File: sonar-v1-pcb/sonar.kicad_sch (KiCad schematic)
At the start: 1 part, among them J101 DF40C-80DS-0.4V51

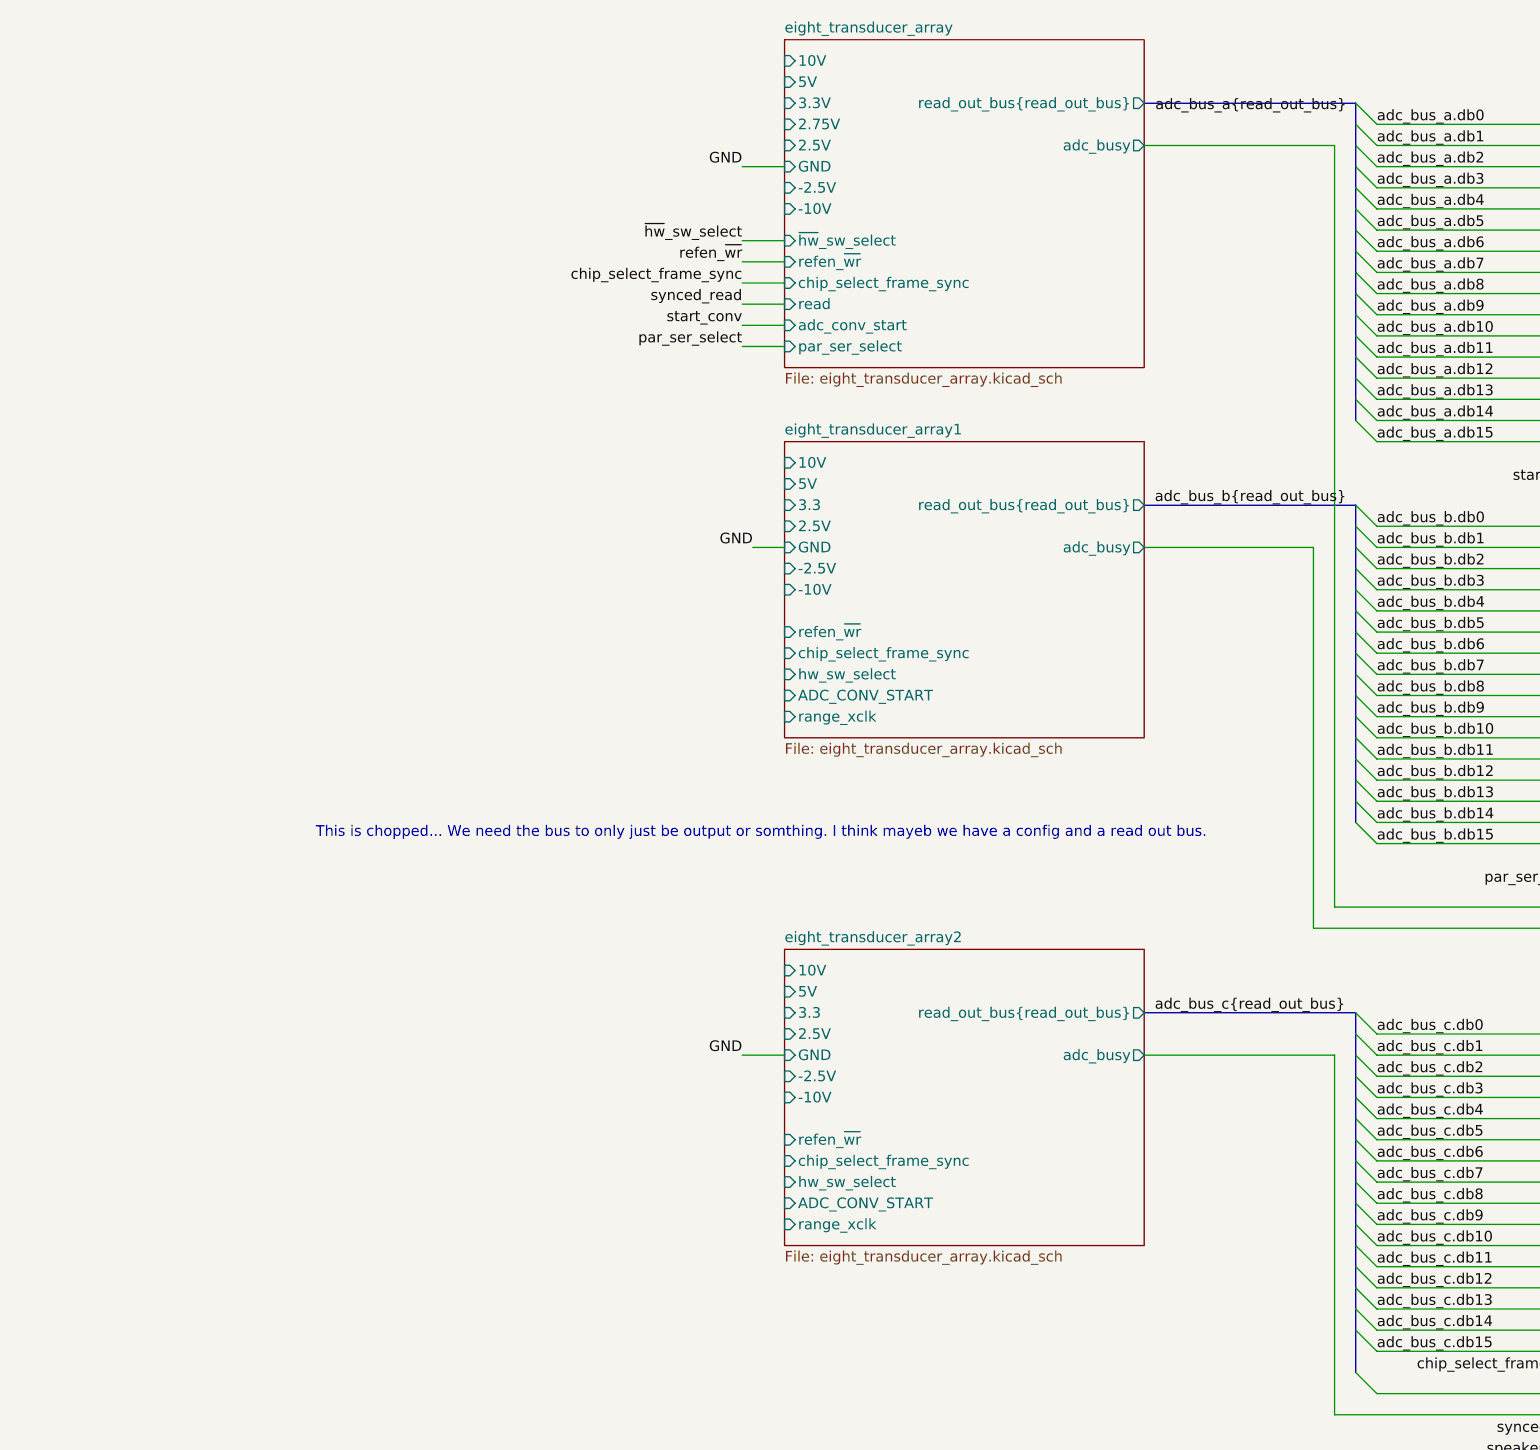
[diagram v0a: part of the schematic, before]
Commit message: Fix pinout
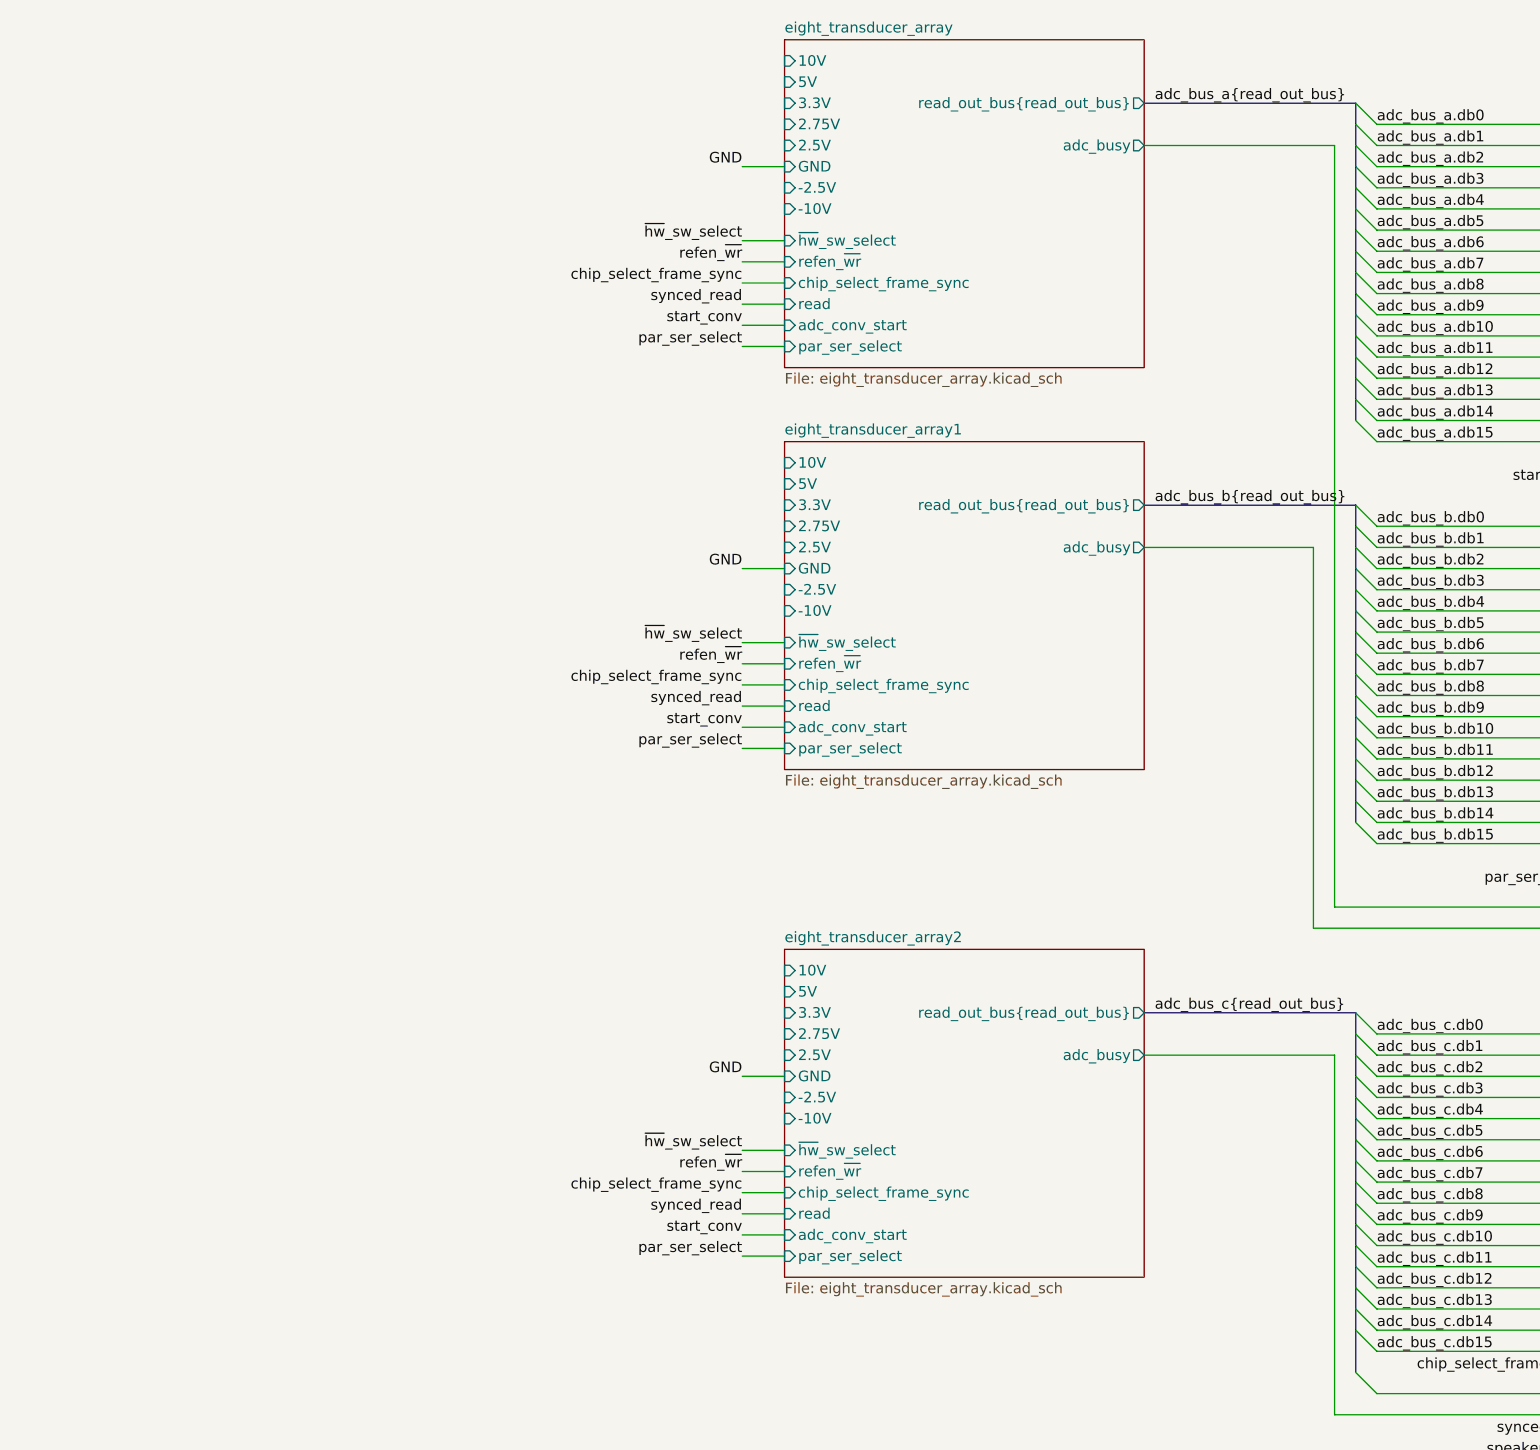
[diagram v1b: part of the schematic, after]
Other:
- sheet eight_transducer_array1 ports: added 2.75V, 3.3V, adc_conv_start, par_ser_select, read, ~{hw}_sw_select; removed 3.3, ADC_CONV_START, hw_sw_select, range_xclk
- sheet eight_transducer_array2 ports: added 2.75V, 3.3V, adc_conv_start, par_ser_select, read, ~{hw}_sw_select; removed 3.3, ADC_CONV_START, hw_sw_select, range_xclk
- note removed: "This is chopped... We need the bus to only just be output or somthing. I think mayeb we have a config and a read out bus."

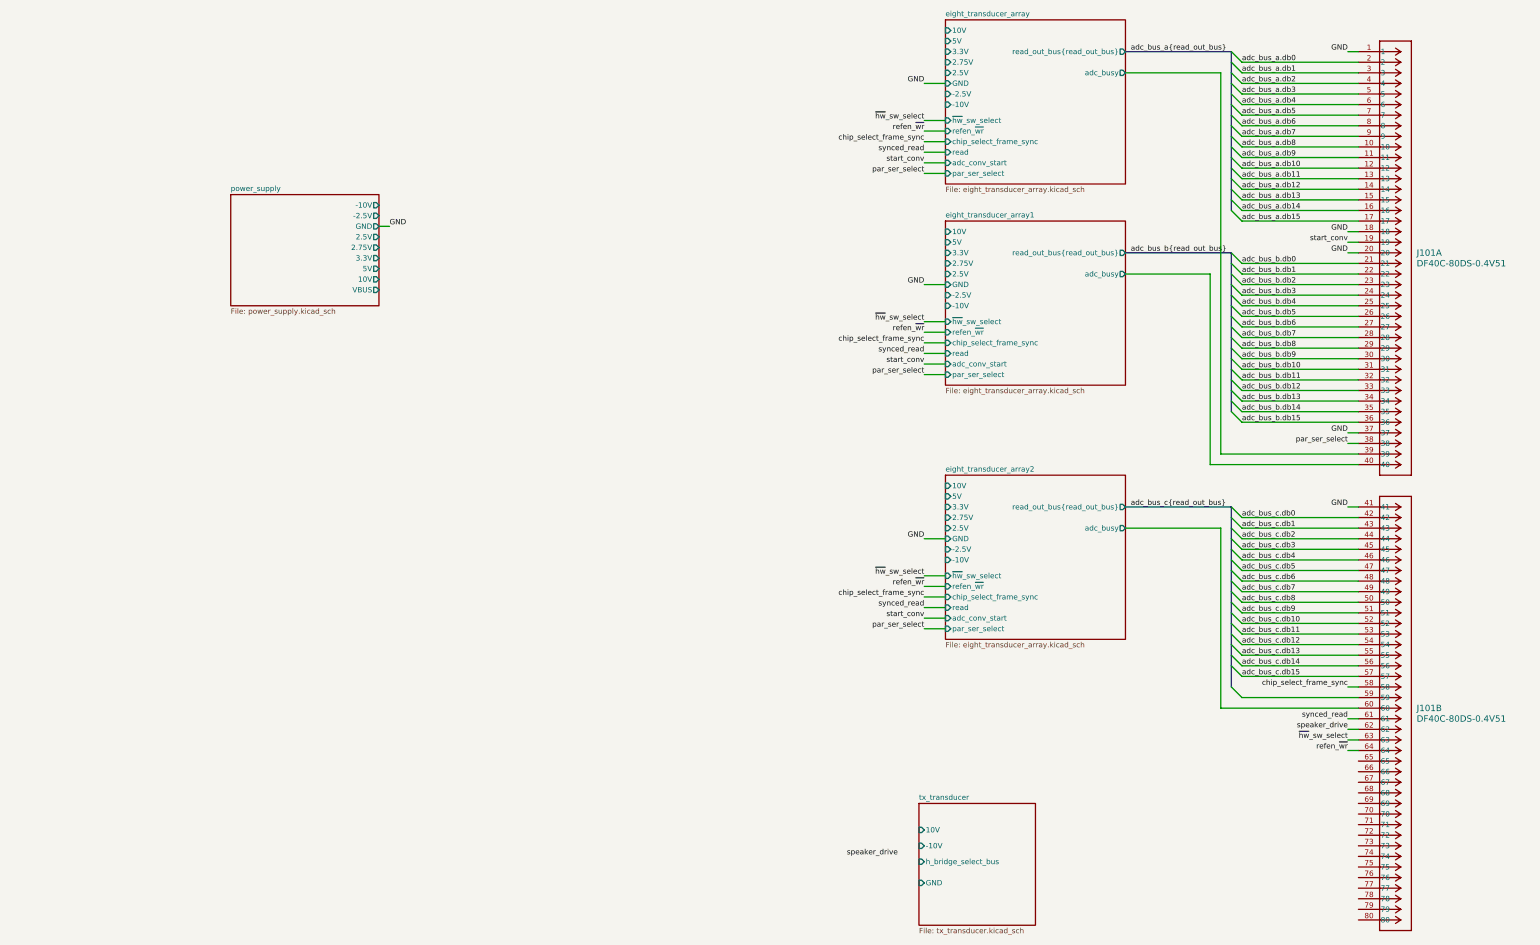
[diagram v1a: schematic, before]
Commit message: Start on power circuitry
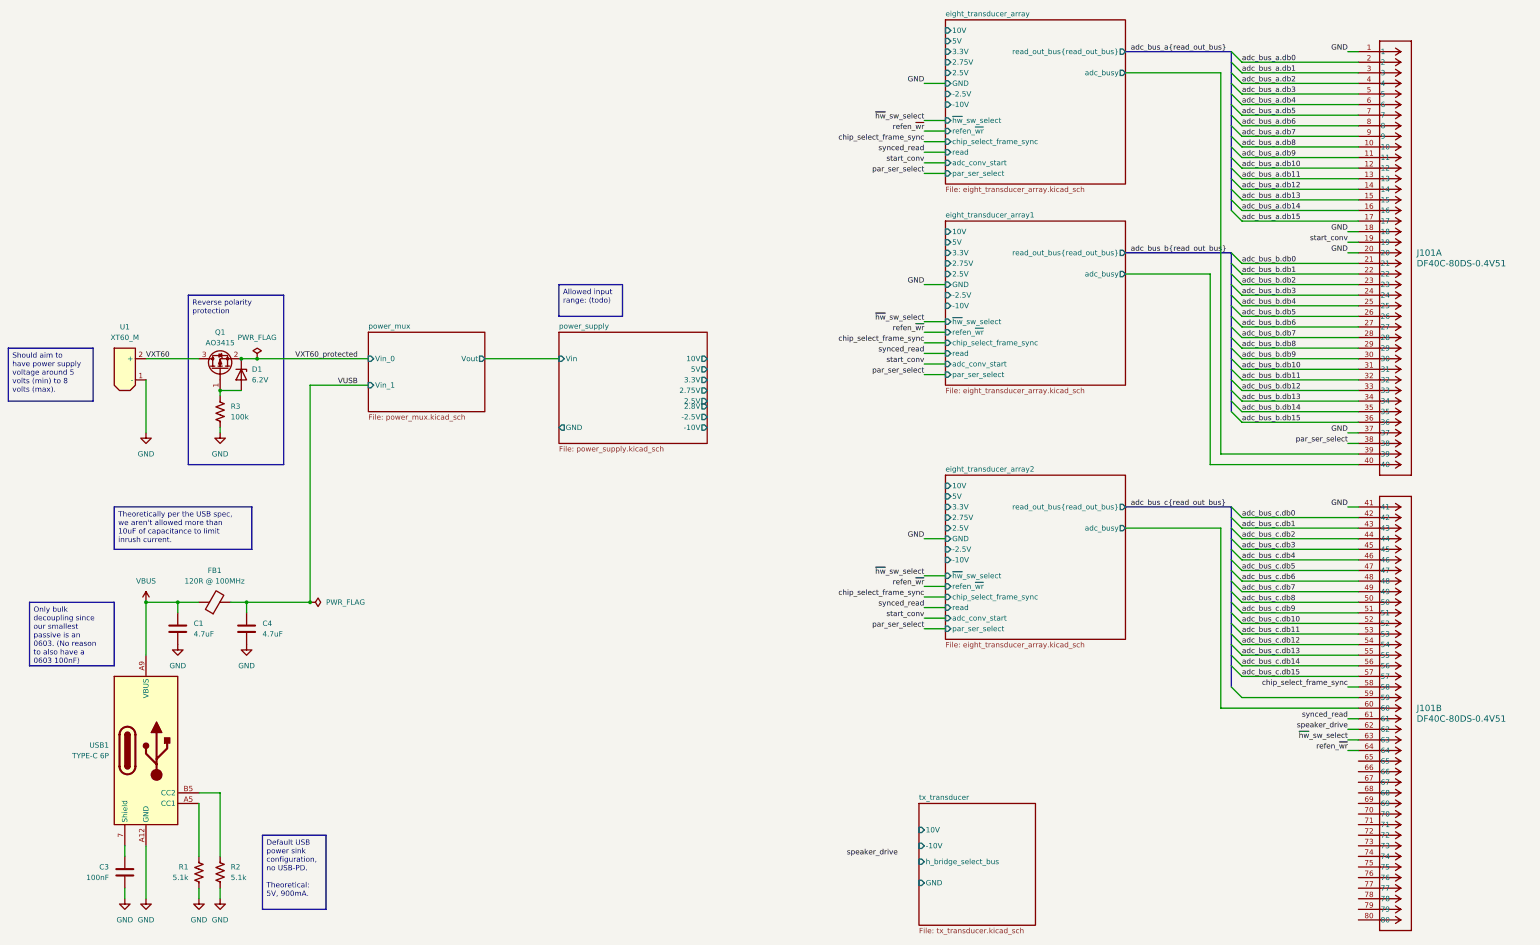
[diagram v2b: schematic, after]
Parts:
- added C1, C4: 4.7uF, Sonar:C_0603_1608Metric, symbol sonar_lib:C_0603_4.7uF
- added C3: 100nF, Sonar:C_0603_1608Metric, symbol sonar_lib:C_0603_100nF
- added D1: 6.2V, Sonar:D_SOD-523, symbol sonar_lib:D_Zener_6.2V_150mW
- added FB1: 120R @ 100MHz, Sonar:L_0603_1608Metric, symbol sonar_lib:FB_0603_120R
- added Q1: AO3415, Sonar:SOT-23, symbol sonar_lib:MOSFET_P-Ch_-20V_4.8A_37mR_-1.2Vth
- added R1, R2: 5.1k, Sonar:R_0603_1608Metric, symbol sonar_lib:R_0603_5.1k
- added R3: 100k, Sonar:R_0603_1608Metric, symbol sonar_lib:R_0603_100k
- added U1: XT60_M, Sonar:XT60_M_VERTICAL, symbol sonar_lib:XT60_M
- added USB1: TYPE-C 6P, Sonar:TYPE-C-SMD_TYPE-C-6P_1, symbol sonar_lib:USB_C_Socket_6P
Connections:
- net GND: now also C1.2, C3.2, C4.2, R1.2, R2.2, R3.2, U1.1 (-), USB1.A12 (GND), USB1.B12 (GND)
- new net: R1.1, USB1.A5 (CC1)
- new net: R2.1, USB1.B5 (CC2)
- new net: D1.2 (A), Q1.1 (G), R3.1
- new net: C3.1, USB1.7 (Shield)
- new net VBUS: C1.1, FB1.1, USB1.A9 (VBUS), USB1.B9 (VBUS)
- new net VUSB: C4.1, FB1.2
- new net VXT60: Q1.3 (D), U1.2 (+)
- new net VXT60_protected: D1.1 (K), Q1.2 (S)
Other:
- added sheet power_mux (power_mux.kicad_sch)
- sheet power_supply ports: added 2.8V, Vin; removed VBUS

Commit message: Do some more power work and add a few components
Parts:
- removed D1: 6.2V, Sonar:D_SOD-523, symbol sonar_lib:D_Zener_6.2V_150mW
- removed Q1: AO3415, Sonar:SOT-23, symbol sonar_lib:MOSFET_P-Ch_-20V_4.8A_37mR_-1.2Vth
- removed R3: 100k, Sonar:R_0603_1608Metric, symbol sonar_lib:R_0603_100k
- added TP1: VXT60, symbol Connector:TestPoint_Probe
- added TP2: VUSB, symbol Connector:TestPoint_Probe
- added TP3: VMUX, symbol Connector:TestPoint_Probe
- added TP4: CC2, symbol Connector:TestPoint_Probe
- added TP5: CC1, symbol Connector:TestPoint_Probe
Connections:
- net VUSB: now also TP2.1
- net VXT60: now also TP1.1
- net power_mux/Vout: now also TP3.1
- net at R1.1, USB1.A5 (CC1): now also TP5.1
- net at R2.1, USB1.B5 (CC2): now also TP4.1
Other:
- sheet power_mux ports: added GND; removed none
- moved on the sheet: C1, C3, C4, FB1, R1, R2, U1, USB1

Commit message: formatting lol
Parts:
- J101: footprint CONN80_DF40C-80DS_HIR -> Sonar:CONN80_DF40C-80DS_HIR
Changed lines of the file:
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@@
 			)
 		)
-		(property "Footprint" "CONN80_DF40C-80DS_HIR"
+		(property "Footprint" "Sonar:CONN80_DF40C-80DS_HIR"
 			(at 341.884 5.588 0)
 			(effects
@@
 			)
 		)
-		(property "Footprint" "CONN80_DF40C-80DS_HIR"
+		(property "Footprint" "Sonar:CONN80_DF40C-80DS_HIR"
 			(at 341.884 114.808 0)
 			(effects
@@
 		)
 		(fill
-			(color 0 0 0 0.0000)
+			(color 194 194 194 1.0000)
 		)
 		(property "Sheetname" "eight_transducer_array2"
@@
 		)
 		(fill
-			(color 0 0 0 0.0000)
+			(color 194 194 194 1.0000)
 		)
 		(property "Sheetname" "eight_transducer_array1"
@@
 		)
 		(fill
-			(color 0 0 0 0.0000)
+			(color 194 194 194 1.0000)
 		)
 		(property "Sheetname" "eight_transducer_array"

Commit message: Update inverting buck boost schematic
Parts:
- J101: footprint Sonar:CONN80_DF40C-80DS_HIR -> CONN80_DF40C-80DS_HIR
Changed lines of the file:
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@@
 			)
 		)
-		(property "Footprint" "Sonar:CONN80_DF40C-80DS_HIR"
+		(property "Footprint" "CONN80_DF40C-80DS_HIR"
 			(at 341.884 5.588 0)
 			(effects
@@
 			)
 		)
-		(property "Footprint" "Sonar:CONN80_DF40C-80DS_HIR"
+		(property "Footprint" "CONN80_DF40C-80DS_HIR"
 			(at 341.884 114.808 0)
 			(effects
@@
 		)
 		(fill
-			(color 194 194 194 1.0000)
+			(color 0 0 0 0.0000)
 		)
 		(property "Sheetname" "eight_transducer_array2"
@@
 		)
 		(fill
-			(color 194 194 194 1.0000)
+			(color 0 0 0 0.0000)
 		)
 		(property "Sheetname" "eight_transducer_array1"
@@
 		)
 		(fill
-			(color 194 194 194 1.0000)
+			(color 0 0 0 0.0000)
 		)
 		(property "Sheetname" "eight_transducer_array"
